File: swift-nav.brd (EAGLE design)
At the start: 53 x 53 mm, 167 parts, among them J1 SMA_EDGE, J6 ZX62-B-5PA, U1 6SLX9FTG256, U10 MAX2769, U12 PT7M8206B33TA5EX, U13 M25PX80, U2 LTC3407A_DFN, U3 STM32-M-64-LQFP, U4 7Q-16.368MBG-T, U5 SMA_PATCH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

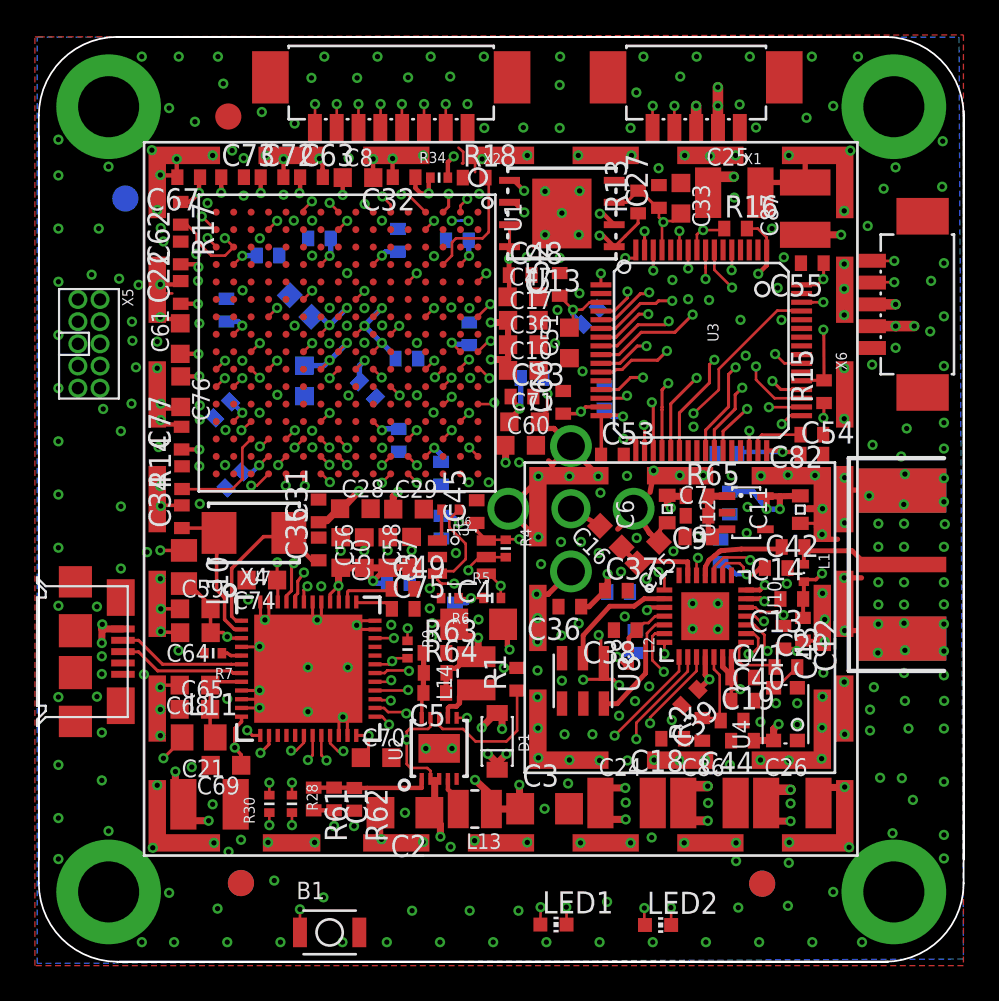
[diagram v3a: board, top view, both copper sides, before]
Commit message: Fix restrict layer on fiducials.
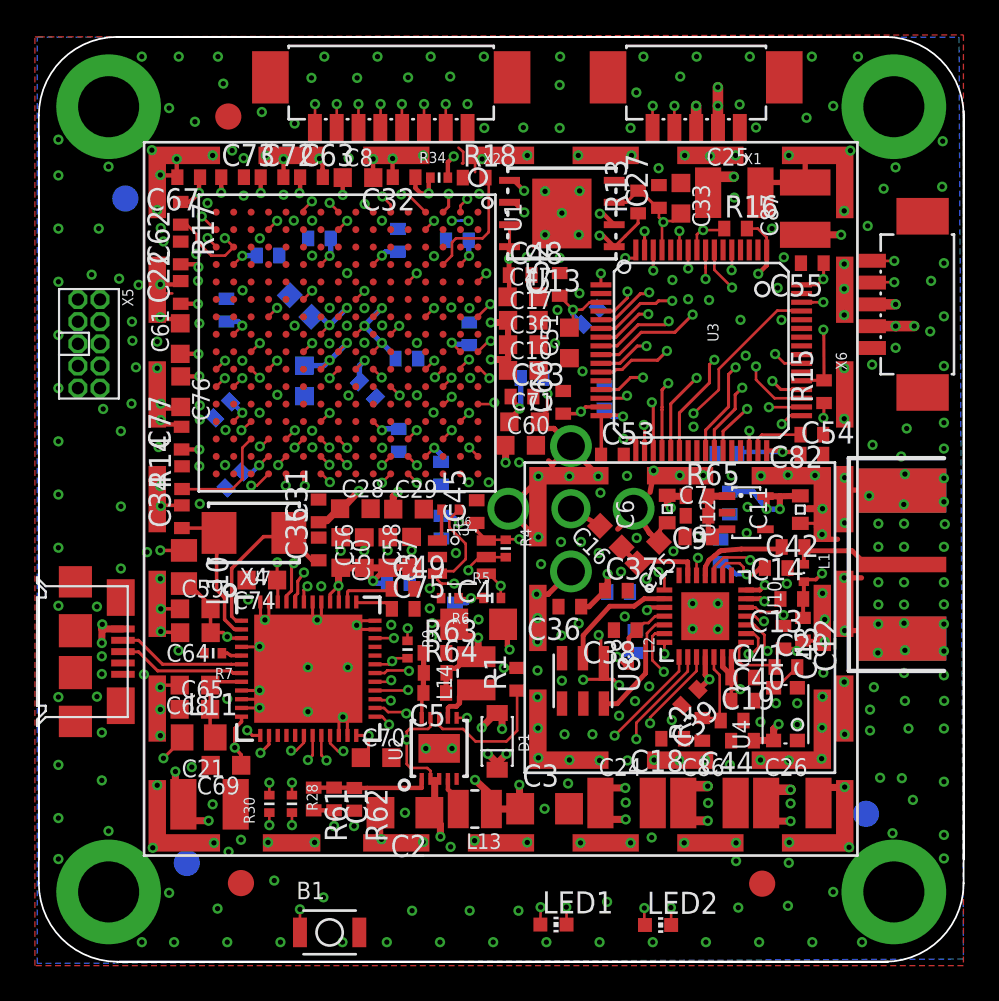
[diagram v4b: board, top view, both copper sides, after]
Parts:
- moved JP5 7.17 mm to (50.8, 11.9)
- moved JP7 3.31 mm to (11.9, 9.06)
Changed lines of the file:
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@@
 <grid distance="0.05" unitdist="mm" unit="mm" style="lines" multiple="1" display="yes" altdistance="0.01" altunitdist="mm" altunit="mm"/>
 <layers>
-<layer number="1" name="Top" color="4" fill="1" visible="yes" active="yes"/>
+<layer number="1" name="Top" color="4" fill="1" visible="no" active="yes"/>
 <layer number="2" name="Route2" color="1" fill="3" visible="no" active="yes"/>
 <layer number="3" name="Route3" color="4" fill="3" visible="no" active="yes"/>
@@
 <layer number="13" name="Route13" color="4" fill="5" visible="no" active="no"/>
 <layer number="14" name="Route14" color="1" fill="6" visible="no" active="yes"/>
-<layer number="15" name="Route15" color="4" fill="6" visible="yes" active="yes"/>
-<layer number="16" name="Bottom" color="1" fill="1" visible="no" active="yes"/>
+<layer number="15" name="Route15" color="4" fill="6" visible="no" active="yes"/>
+<layer number="16" name="Bottom" color="1" fill="1" visible="yes" active="yes"/>
 <layer number="17" name="Pads" color="2" fill="1" visible="yes" active="yes"/>
 <layer number="18" name="Vias" color="2" fill="1" visible="yes" active="yes"/>
 <layer number="19" name="Unrouted" color="6" fill="1" visible="yes" active="yes"/>
 <layer number="20" name="Dimension" color="15" fill="1" visible="yes" active="yes"/>
-<layer number="21" name="tPlace" color="7" fill="1" visible="yes" active="yes"/>
-<layer number="22" name="bPlace" color="7" fill="1" visible="no" active="yes"/>
-<layer number="23" name="tOrigins" color="15" fill="1" visible="yes" active="yes"/>
-<layer number="24" name="bOrigins" color="15" fill="1" visible="no" active="yes"/>
+<layer number="21" name="tPlace" color="7" fill="1" visible="no" active="yes"/>
+<layer number="22" name="bPlace" color="7" fill="1" visible="yes" active="yes"/>
+<layer number="23" name="tOrigins" color="15" fill="1" visible="no" active="yes"/>
+<layer number="24" name="bOrigins" color="15" fill="1" visible="yes" active="yes"/>
 <layer number="25" name="tNames" color="7" fill="1" visible="no" active="yes"/>
 <layer number="26" name="bNames" color="7" fill="1" visible="no" active="yes"/>
@@
 <layer number="110" name="fp0" color="7" fill="1" visible="no" active="yes"/>
 <layer number="111" name="Text" color="15" fill="1" visible="no" active="yes"/>
+<layer number="112" name="2Restrict" color="7" fill="1" visible="no" active="yes"/>
 <layer number="116" name="Patch_BOT" color="9" fill="4" visible="no" active="yes"/>
-<layer number="121" name="_tplace" color="14" fill="1" visible="yes" active="yes"/>
-<layer number="122" name="_bplace" color="14" fill="1" visible="no" active="yes"/>
+<layer number="121" name="_tplace" color="14" fill="1" visible="no" active="yes"/>
+<layer number="122" name="_bplace" color="14" fill="1" visible="yes" active="yes"/>
 <layer number="123" name="tTestmark" color="7" fill="1" visible="no" active="yes"/>
 <layer number="124" name="bTestmark" color="7" fill="1" visible="no" active="yes"/>
@@
 <element name="R28" library="pel_dipol_comp" package="0402-RES" value="150" x="17.907" y="12.446" rot="R270"/>
 <element name="R30" library="pel_dipol_comp" package="0402-RES" value="150" x="16.6116" y="12.446" rot="R90"/>
-<element name="JP5" library="aspirin" package="FIDUCIAL-1.5X3" value="FIDUCIAL1.5X3" x="44.854" y="7.872" rot="MR180"/>
+<element name="JP5" library="aspirin" package="FIDUCIAL-1.5X3" value="FIDUCIAL1.5X3" x="50.804" y="11.872" rot="MR180"/>
 <element name="JP6" library="aspirin" package="FIDUCIAL-1.5X3" value="FIDUCIAL1.5X3" x="8.3586" y="47.138" rot="MR270"/>
-<element name="JP7" library="aspirin" package="FIDUCIAL-1.5X3" value="FIDUCIAL1.5X3" x="14.984" y="7.91" rot="MR270"/>
+<element name="JP7" library="aspirin" package="FIDUCIAL-1.5X3" value="FIDUCIAL1.5X3" x="11.884" y="9.06" rot="MR270"/>
 <element name="JP8" library="aspirin" package="FIDUCIAL-1.5X3" value="FIDUCIAL1.5X3" x="44.854" y="7.873" rot="R90"/>
 <element name="JP9" library="aspirin" package="FIDUCIAL-1.5X3" value="FIDUCIAL1.5X3" x="14.2586" y="51.838" rot="R90"/>

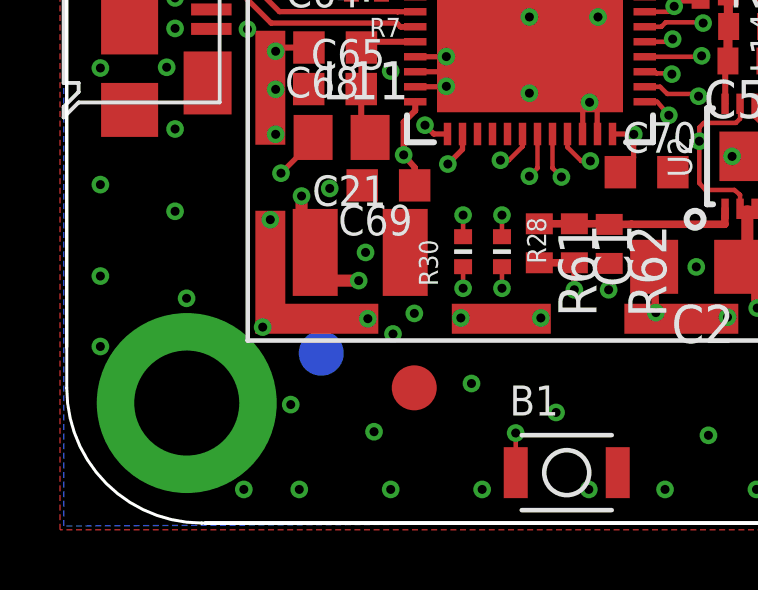
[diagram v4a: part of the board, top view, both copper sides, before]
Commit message: Move fiducial
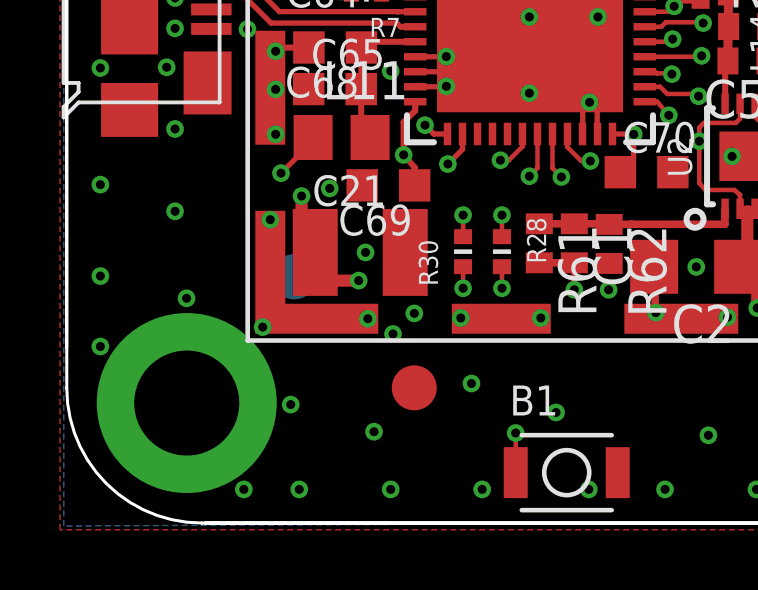
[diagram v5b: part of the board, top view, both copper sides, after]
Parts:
- moved JP7 2.70 mm to (11.0, 11.6)
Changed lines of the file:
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@@
 <layer number="40" name="bKeepout" color="1" fill="11" visible="no" active="yes"/>
 <layer number="41" name="tRestrict" color="4" fill="10" visible="no" active="yes"/>
-<layer number="42" name="bRestrict" color="1" fill="10" visible="no" active="yes"/>
+<layer number="42" name="bRestrict" color="1" fill="10" visible="yes" active="yes"/>
 <layer number="43" name="vRestrict" color="2" fill="10" visible="no" active="yes"/>
 <layer number="44" name="Drills" color="7" fill="1" visible="no" active="yes"/>
@@
 <element name="JP5" library="aspirin" package="FIDUCIAL-1.5X3" value="FIDUCIAL1.5X3" x="50.804" y="11.872" rot="MR180"/>
 <element name="JP6" library="aspirin" package="FIDUCIAL-1.5X3" value="FIDUCIAL1.5X3" x="8.3586" y="47.138" rot="MR270"/>
-<element name="JP7" library="aspirin" package="FIDUCIAL-1.5X3" value="FIDUCIAL1.5X3" x="11.884" y="9.06" rot="MR270"/>
+<element name="JP7" library="aspirin" package="FIDUCIAL-1.5X3" value="FIDUCIAL1.5X3" x="10.984" y="11.61" rot="MR270"/>
 <element name="JP8" library="aspirin" package="FIDUCIAL-1.5X3" value="FIDUCIAL1.5X3" x="44.854" y="7.873" rot="R90"/>
 <element name="JP9" library="aspirin" package="FIDUCIAL-1.5X3" value="FIDUCIAL1.5X3" x="14.2586" y="51.838" rot="R90"/>

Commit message: Move a different fiducial.
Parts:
- moved JP10 3.34 mm to (12.2, 6.01)
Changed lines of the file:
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@@
 <grid distance="0.05" unitdist="mm" unit="mm" style="lines" multiple="1" display="yes" altdistance="0.01" altunitdist="mm" altunit="mm"/>
 <layers>
-<layer number="1" name="Top" color="4" fill="1" visible="no" active="yes"/>
+<layer number="1" name="Top" color="4" fill="1" visible="yes" active="yes"/>
 <layer number="2" name="Route2" color="1" fill="3" visible="no" active="yes"/>
 <layer number="3" name="Route3" color="4" fill="3" visible="no" active="yes"/>
@@
 <layer number="14" name="Route14" color="1" fill="6" visible="no" active="yes"/>
 <layer number="15" name="Route15" color="4" fill="6" visible="no" active="yes"/>
-<layer number="16" name="Bottom" color="1" fill="1" visible="yes" active="yes"/>
+<layer number="16" name="Bottom" color="1" fill="1" visible="no" active="yes"/>
 <layer number="17" name="Pads" color="2" fill="1" visible="yes" active="yes"/>
 <layer number="18" name="Vias" color="2" fill="1" visible="yes" active="yes"/>
 <layer number="19" name="Unrouted" color="6" fill="1" visible="yes" active="yes"/>
 <layer number="20" name="Dimension" color="15" fill="1" visible="yes" active="yes"/>
-<layer number="21" name="tPlace" color="7" fill="1" visible="no" active="yes"/>
-<layer number="22" name="bPlace" color="7" fill="1" visible="yes" active="yes"/>
-<layer number="23" name="tOrigins" color="15" fill="1" visible="no" active="yes"/>
-<layer number="24" name="bOrigins" color="15" fill="1" visible="yes" active="yes"/>
+<layer number="21" name="tPlace" color="7" fill="1" visible="yes" active="yes"/>
+<layer number="22" name="bPlace" color="7" fill="1" visible="no" active="yes"/>
+<layer number="23" name="tOrigins" color="15" fill="1" visible="yes" active="yes"/>
+<layer number="24" name="bOrigins" color="15" fill="1" visible="no" active="yes"/>
 <layer number="25" name="tNames" color="7" fill="1" visible="no" active="yes"/>
 <layer number="26" name="bNames" color="7" fill="1" visible="no" active="yes"/>
@@
 <layer number="40" name="bKeepout" color="1" fill="11" visible="no" active="yes"/>
 <layer number="41" name="tRestrict" color="4" fill="10" visible="no" active="yes"/>
-<layer number="42" name="bRestrict" color="1" fill="10" visible="yes" active="yes"/>
+<layer number="42" name="bRestrict" color="1" fill="10" visible="no" active="yes"/>
 <layer number="43" name="vRestrict" color="2" fill="10" visible="no" active="yes"/>
 <layer number="44" name="Drills" color="7" fill="1" visible="no" active="yes"/>
@@
 <layer number="112" name="2Restrict" color="7" fill="1" visible="no" active="yes"/>
 <layer number="116" name="Patch_BOT" color="9" fill="4" visible="no" active="yes"/>
-<layer number="121" name="_tplace" color="14" fill="1" visible="no" active="yes"/>
-<layer number="122" name="_bplace" color="14" fill="1" visible="yes" active="yes"/>
+<layer number="121" name="_tplace" color="14" fill="1" visible="yes" active="yes"/>
+<layer number="122" name="_bplace" color="14" fill="1" visible="no" active="yes"/>
 <layer number="123" name="tTestmark" color="7" fill="1" visible="no" active="yes"/>
 <layer number="124" name="bTestmark" color="7" fill="1" visible="no" active="yes"/>
@@
 <element name="JP8" library="aspirin" package="FIDUCIAL-1.5X3" value="FIDUCIAL1.5X3" x="44.854" y="7.873" rot="R90"/>
 <element name="JP9" library="aspirin" package="FIDUCIAL-1.5X3" value="FIDUCIAL1.5X3" x="14.2586" y="51.838" rot="R90"/>
-<element name="JP10" library="aspirin" package="FIDUCIAL-1.5X3" value="FIDUCIAL1.5X3" x="14.984" y="7.907" rot="R90"/>
+<element name="JP10" library="aspirin" package="FIDUCIAL-1.5X3" value="FIDUCIAL1.5X3" x="12.234" y="6.007" rot="R90"/>
 <element name="C15" library="rcl" package="C0603K" value="DNP" x="38.3206375" y="26.8416375" rot="R225"/>
 <element name="LED1" library="led" package="CHIP-LED0603" value="RED" x="32.893" y="5.5292" rot="R270"/>
@@
 <via x="7.0104" y="16.5354" extent="1-16" drill="0.3"/>
 <via x="7.0104" y="13.7922" extent="1-16" drill="0.3"/>
-<via x="13.6428" y="6.4444" extent="1-16" drill="0.3"/>
+<via x="13.9928" y="6.7944" extent="1-16" drill="0.3"/>
 <via x="19.7104" y="7.0866" extent="1-16" drill="0.3"/>
 <via x="24.7904" y="6.3246" extent="1-16" drill="0.3"/>

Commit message: VUSB pulldown + other shiz
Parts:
- added R8: 10K, pel_dipol_comp:0402-RES
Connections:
- net GND: now also R8.P$1
- net V_USB: now also R8.P$2
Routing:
- net V_USB: track 112.2 -> 116.2 mm, vias 5 -> 6
- net SPI2MISO: track 52.8 -> 54.1 mm
- net MAX_I1: track 25.6 -> 26.2 mm
- net GND: vias 396 -> 405

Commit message: UART6 solder jumper for bus contention.
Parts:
- added SJ1: SOLDERJUMPERTRACE, SparkFun-Passives:SJ_2S-TRACE
- moved R8 3.30 mm to (20.4, 14.4), turned to 180 degrees
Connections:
- new net N$2: SJ1.1, U7.14
- net UART6_TX: now also SJ1.2; no longer U7.14
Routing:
- net FTDI_NRST: track 105.9 -> 110.2 mm
- net GND: track 94.9 -> 97.8 mm
- net N$2: track 0.00 -> 1.67 mm
- net V_USB: track 116.2 -> 115.0 mm
- net FTDI_ADBUS6: track 22.0 -> 21.1 mm
- net UART6_TX: track 51.3 -> 52.1 mm
- net FTDI_ADBUS7: track 25.6 -> 25.0 mm
